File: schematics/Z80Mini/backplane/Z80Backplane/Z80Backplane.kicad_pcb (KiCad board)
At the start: 2 copper layers, 151.1 x 110.5 mm, 11 parts, among them J1 Conn_02x20_Odd_Even, J2 Conn_02x20_Odd_Even, J3 Conn_02x20_Odd_Even, J4 Conn_02x20_Odd_Even, U1 L7805

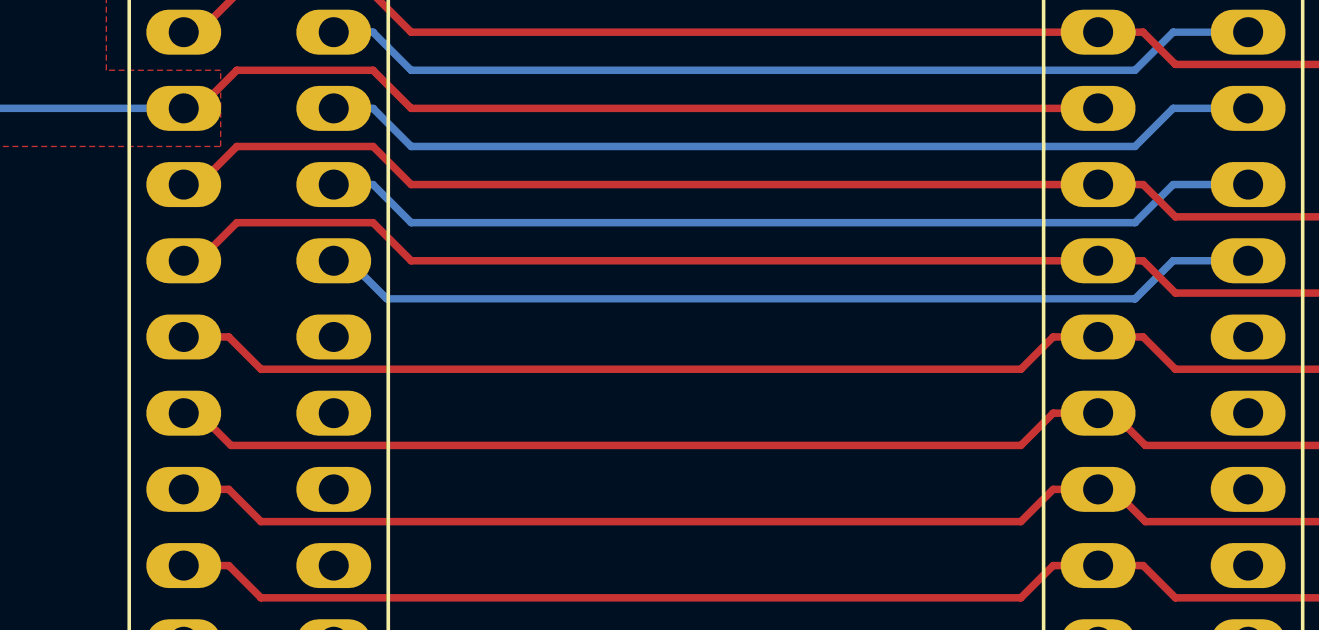
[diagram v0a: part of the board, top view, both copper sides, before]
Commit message: Added new code for core written in C with Z88DK
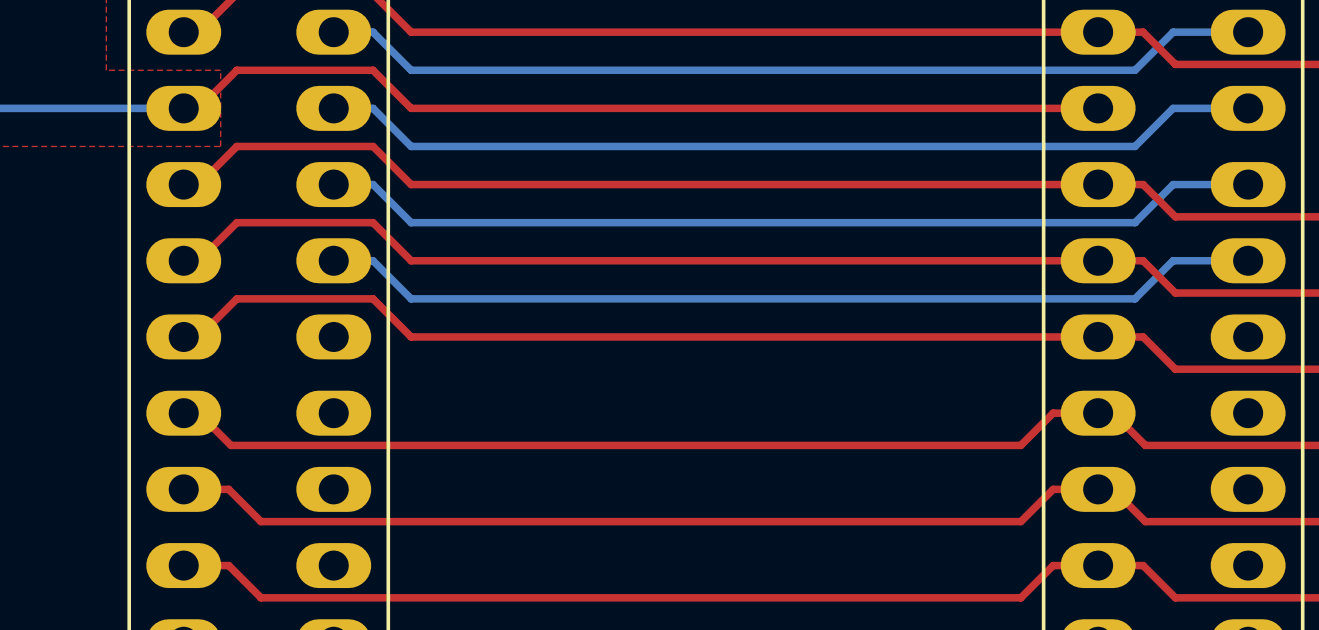
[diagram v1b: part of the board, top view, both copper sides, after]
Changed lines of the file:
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@@
-(kicad_pcb (version 20171130) (host pcbnew "(5.1.2)-1")
+(kicad_pcb (version 20171130) (host pcbnew "(5.1.4)-1")
   (general
     (thickness 1.6)
     (drawings 4)
-    (tracks 377)
+    (tracks 378)
     (zones 0)
     (modules 11)
@@
     (trace_clearance 0.2)
     (zone_clearance 0.508)
-    (zone_45_only no)
+    (zone_45_only yes)
     (trace_min 0.2)
     (via_size 0.8)
@@
   (segment (start 129.81 82.55) (end 130.88501 83.62501) (width 0.25) (layer F.Cu) (net 22))
   (segment (start 128.31 82.55) (end 129.81 82.55) (width 0.25) (layer F.Cu) (net 22))
-  (segment (start 93.79 80.01) (end 95.29 80.01) (width 0.25) (layer F.Cu) (net 24))
-  (segment (start 92.71499 81.08501) (end 93.79 80.01) (width 0.25) (layer F.Cu) (net 24))
-  (segment (start 67.38501 81.08501) (end 92.71499 81.08501) (width 0.25) (layer F.Cu) (net 24))
-  (segment (start 66.31 80.01) (end 67.38501 81.08501) (width 0.25) (layer F.Cu) (net 24))
-  (segment (start 64.81 80.01) (end 66.31 80.01) (width 0.25) (layer F.Cu) (net 24))
   (segment (start 126.81 80.01) (end 128.31 80.01) (width 0.25) (layer F.Cu) (net 24))
   (segment (start 125.73499 81.08501) (end 126.81 80.01) (width 0.25) (layer F.Cu) (net 24))
@@
   (segment (start 129.81 80.01) (end 130.88501 81.08501) (width 0.25) (layer F.Cu) (net 24))
   (segment (start 128.31 80.01) (end 129.81 80.01) (width 0.25) (layer F.Cu) (net 24))
+  (segment (start 65.31 80.01) (end 66.58 78.74) (width 0.25) (layer F.Cu) (net 24))
+  (segment (start 64.81 80.01) (end 65.31 80.01) (width 0.25) (layer F.Cu) (net 24))
+  (segment (start 66.58 78.74) (end 71.12 78.74) (width 0.25) (layer F.Cu) (net 24))
+  (segment (start 72.39 80.01) (end 95.29 80.01) (width 0.25) (layer F.Cu) (net 24))
+  (segment (start 71.12 78.74) (end 72.39 80.01) (width 0.25) (layer F.Cu) (net 24))
   (segment (start 126.81 77.47) (end 128.31 77.47) (width 0.25) (layer F.Cu) (net 26))
   (segment (start 125.73499 78.54501) (end 126.81 77.47) (width 0.25) (layer F.Cu) (net 26))
@@
   (segment (start 72.39 77.47) (end 95.29 77.47) (width 0.25) (layer F.Cu) (net 26))
   (segment (start 71.12 76.2) (end 72.39 77.47) (width 0.25) (layer F.Cu) (net 26))
-  (segment (start 70.31 77.47) (end 71.58 78.74) (width 0.25) (layer B.Cu) (net 27))
   (segment (start 69.81 77.47) (end 70.31 77.47) (width 0.25) (layer B.Cu) (net 27))
-  (segment (start 71.58 78.74) (end 96.52 78.74) (width 0.25) (layer B.Cu) (net 27))
   (segment (start 97.79 77.47) (end 100.29 77.47) (width 0.25) (layer B.Cu) (net 27))
   (segment (start 96.52 78.74) (end 97.79 77.47) (width 0.25) (layer B.Cu) (net 27))
+  (segment (start 70.31 77.47) (end 71.12 77.47) (width 0.25) (layer B.Cu) (net 27))
+  (segment (start 71.12 77.47) (end 72.39 78.74) (width 0.25) (layer B.Cu) (net 27))
+  (segment (start 72.39 78.74) (end 96.52 78.74) (width 0.25) (layer B.Cu) (net 27))
   (segment (start 126.81 74.93) (end 128.31 74.93) (width 0.25) (layer F.Cu) (net 28))
   (segment (start 125.73499 76.00501) (end 126.81 74.93) (width 0.25) (layer F.Cu) (net 28))
@@
   (segment (start 49.53 74.93) (end 48.26 76.2) (width 1) (layer F.Cu) (net 41))
   (segment (start 40.64 49.53) (end 40.64 44.45) (width 0.25) (layer F.Cu) (net 42))
-  (zone (net 7) (net_name GND) (layer B.Cu) (hatch edge 0.508)
+  (zone (net 7) (net_name GND) (layer B.Cu) (hatch none 0.508)
     (connect_pads (clearance 0.508))
     (min_thickness 0.254)

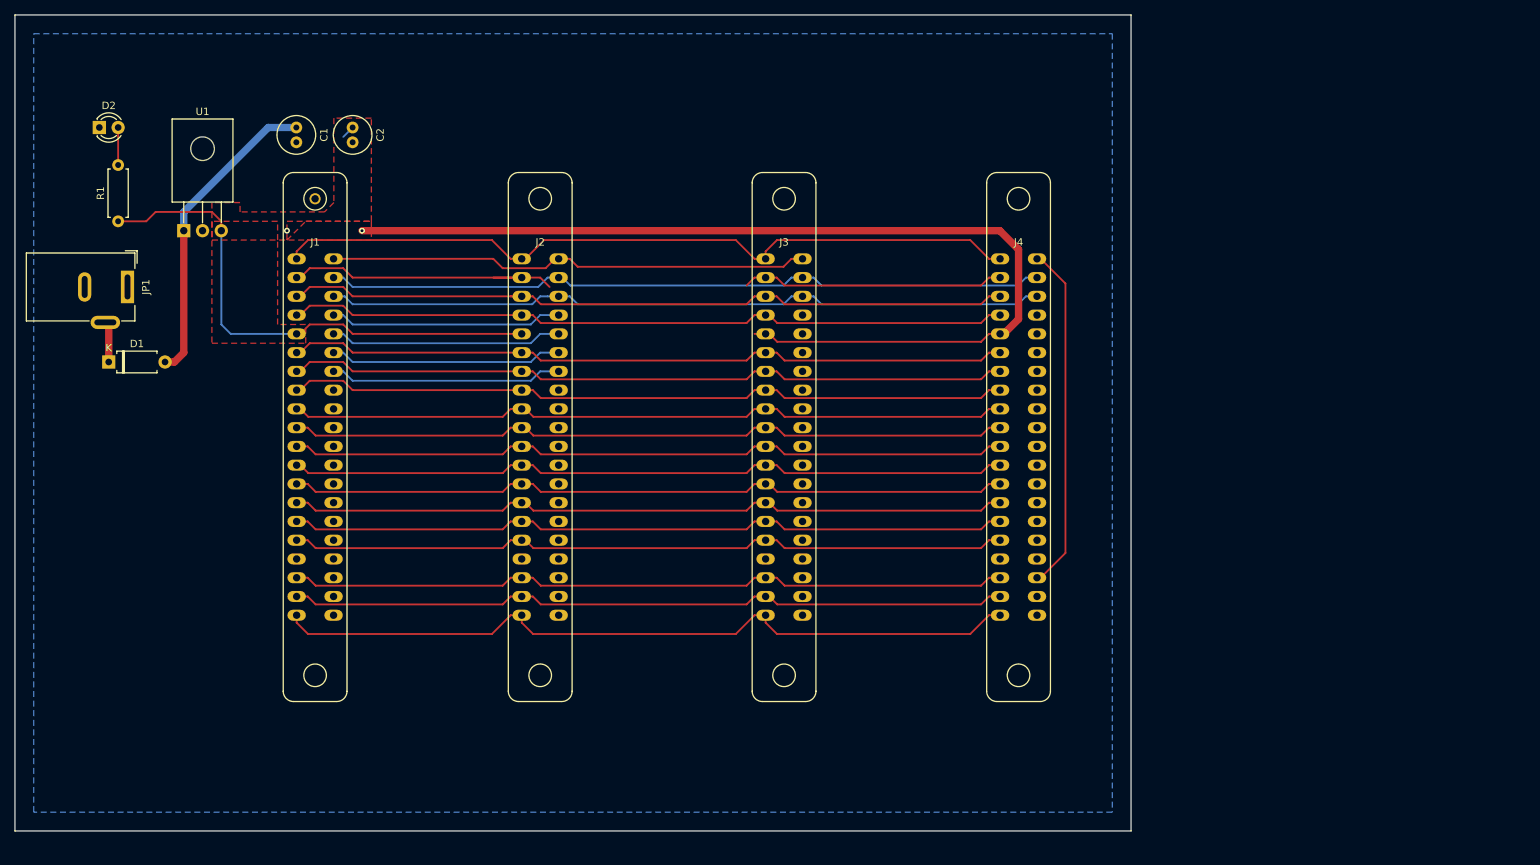
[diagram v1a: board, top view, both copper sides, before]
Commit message: Testing C routines for VDP and keyboard. Generated backplane gerber files
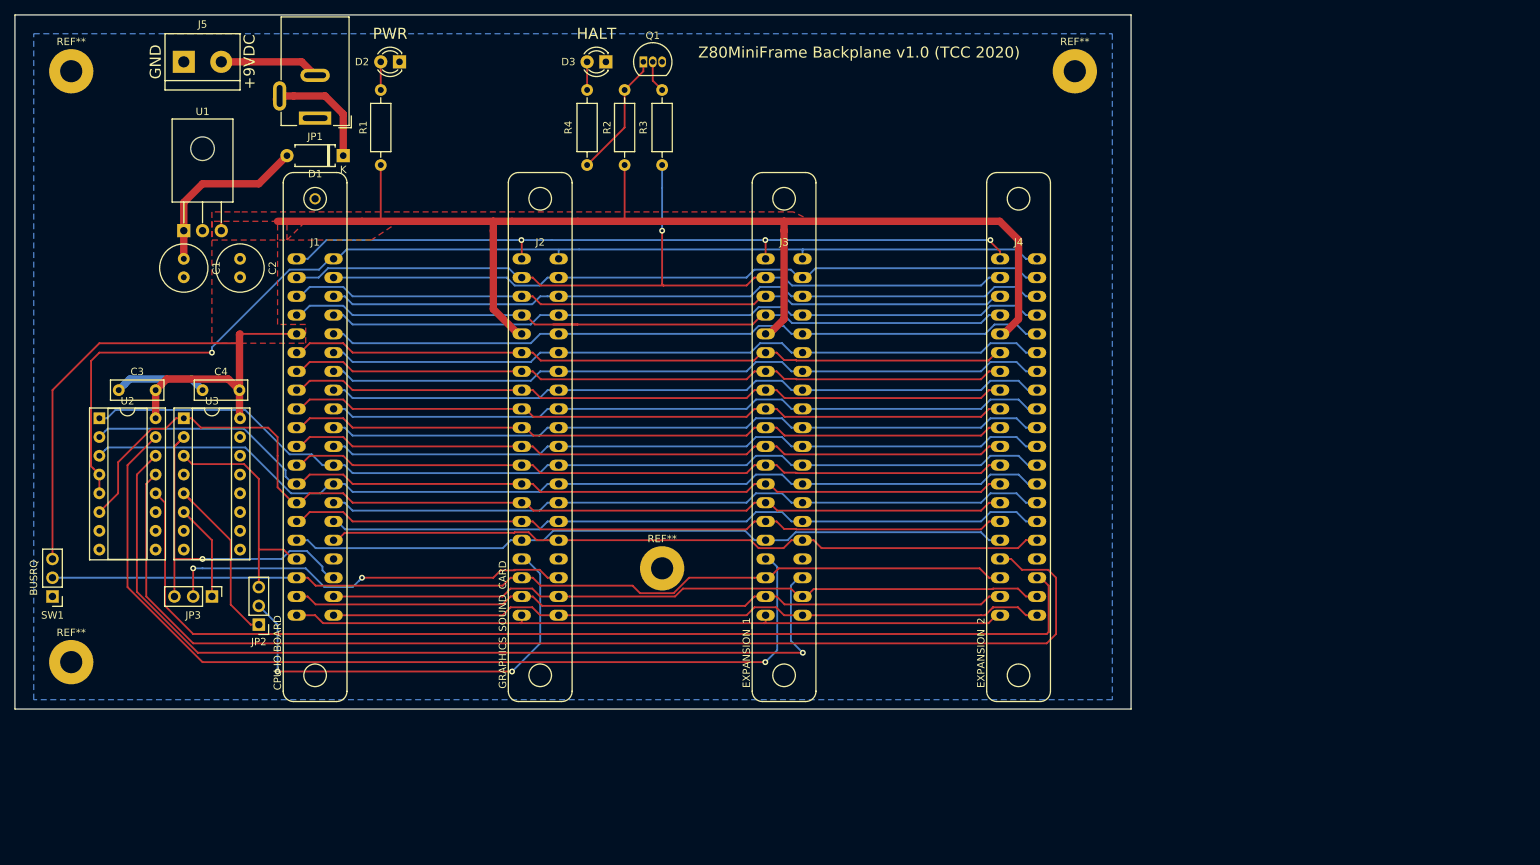
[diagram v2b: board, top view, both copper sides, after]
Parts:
- added C3: 100nF, Capacitor_THT:C_Disc_D7.0mm_W2.5mm_P5.00mm, F.Cu at (40.7, 80.0)
- added C4: 100nF, Capacitor_THT:C_Disc_D7.0mm_W2.5mm_P5.00mm, F.Cu at (52.1, 80.0)
- added D3: LED_HALT, LED_THT:LED_D3.0mm, F.Cu at (106.7, 35.6)
- added J5: Screw_Terminal_01x02, TerminalBlock:TerminalBlock_bornier-2_P5.08mm, F.Cu at (49.5, 35.6)
- added JP2: Jumper_NC_Dual, Connector_PinHeader_2.54mm:PinHeader_1x03_P2.54mm_Vertical, F.Cu at (59.7, 111.8)
- added JP3: Jumper_NC_Dual, Connector_PinHeader_2.54mm:PinHeader_1x03_P2.54mm_Vertical, F.Cu at (53.3, 108.0)
- added Q1: BC337, Package_TO_SOT_THT:TO-92_Inline, F.Cu at (111.8, 35.6)
- added R2: 330R, Resistor_THT:R_Axial_DIN0207_L6.3mm_D2.5mm_P10.16mm_Horizontal, F.Cu at (109.2, 49.5)
- added R3: 1K, Resistor_THT:R_Axial_DIN0207_L6.3mm_D2.5mm_P10.16mm_Horizontal, F.Cu at (114.3, 39.4)
- added R4: 330R, Resistor_THT:R_Axial_DIN0207_L6.3mm_D2.5mm_P10.16mm_Horizontal, F.Cu at (104.1, 39.4)
- added REF**: MountingHole_3mm_Pad, MountingHole:MountingHole_3mm_Pad, F.Cu at (114.3, 104.1)
- added REF**: MountingHole_3mm_Pad, MountingHole:MountingHole_3mm_Pad, F.Cu at (34.3, 116.8)
- added REF**: MountingHole_3mm_Pad, MountingHole:MountingHole_3mm_Pad, F.Cu at (34.3, 36.8)
- added REF**: MountingHole_3mm_Pad, MountingHole:MountingHole_3mm_Pad, F.Cu at (170.2, 36.8)
- added SW1: SW_SPDT, Connector_PinHeader_2.54mm:PinHeader_1x03_P2.54mm_Vertical, F.Cu at (31.8, 108.0)
- added U2: 74LS138, Package_DIP:DIP-16_W7.62mm_Socket, F.Cu at (38.1, 83.8)
- added U3: 74LS139, Package_DIP:DIP-16_W7.62mm_Socket, F.Cu at (49.5, 83.8)
- C1, C2: footprint Capacitor_THT:C_Radial_D5.0mm_H11.0mm_P2.00mm -> Capacitor_THT:C_Radial_D6.3mm_H5.0mm_P2.50mm
- J1: value Conn_02x20_Odd_Even -> CPU-IO BOARD
- J2: value Conn_02x20_Odd_Even -> GRAPHICS_SOUND_CARD
- J3: value Conn_02x20_Odd_Even -> EXPANSION_1
- J4: value Conn_02x20_Odd_Even -> EXPANSION_2
- R1: footprint Resistor_THT:R_Axial_DIN0207_L6.3mm_D2.5mm_P7.62mm_Horizontal -> Resistor_THT:R_Axial_DIN0207_L6.3mm_D2.5mm_P10.16mm_Horizontal
- moved D1 42.3 mm to (71.1, 48.3), turned to 180 degrees
- moved D2 41.6 mm to (78.7, 35.6), turned to 180 degrees
- moved R1 36.4 mm to (76.2, 49.5)
- moved JP1 34.2 mm to (67.3, 43.2), turned to 180 degrees
- moved C2 23.4 mm to (57.1, 62.2)
- moved C1 23.4 mm to (49.5, 62.2)
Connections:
- J1 pad 33: GND -> /VDP_SEL
- J1 pad 36: /IORQ -> /SND_SEL
- J2 pad 33: GND -> Net-(J2-Pad33)
- J2 pad 36: /IORQ -> Net-(J2-Pad36)
- J3 pad 33: GND -> Net-(J3-Pad33)
- J3 pad 36: /IORQ -> Net-(J3-Pad36)
- J4 pad 33: GND -> Net-(J4-Pad33)
- J4 pad 36: /IORQ -> Net-(J4-Pad36)
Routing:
- net Net-(J4-Pad33): track 0.00 -> 160.1 mm
- net Net-(J4-Pad36): track 0.00 -> 145.9 mm
- net /A7: track 0.00 -> 135.0 mm
- net /A5: track 0.00 -> 134.5 mm
- net Net-(J3-Pad33): track 0.00 -> 128.1 mm, vias 0 -> 1
- net Net-(J3-Pad36): track 0.00 -> 124.8 mm, vias 0 -> 1
- net /A11: track 0.00 -> 100.2 mm
- net /BUSACK: track 0.00 -> 99.9 mm
- net /WR: track 0.00 -> 99.7 mm
- net /A3: track 0.00 -> 99.7 mm
- net /D6: track 0.00 -> 99.7 mm
- net /A14: track 0.00 -> 99.4 mm
- net /A9: track 0.00 -> 99.2 mm
- net /A1: track 0.00 -> 99.2 mm
- net /INT: track 0.00 -> 99.0 mm
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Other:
- board size 151.1 x 110.5 mm -> 151.1 x 94 mm
- board text added: "+9VDC"
- board text added: "BUSRQ"
- board text added: "GND"
- board text added: "HALT"
- board text added: "PWR"
- board text added: "Z80MiniFrame Backplane v1.0 (TCC 2020)"

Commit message: Latest changes and added CTC initialization and routine to flash cursor
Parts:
- moved J4 3.81 mm to (158.8, 86.4)
- moved J3 2.54 mm to (128.3, 86.4)
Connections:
- J1 pad 2: /IORQ -> /NMI
- J1 pad 4: /NMI -> /WAIT
- J1 pad 6: /WAIT -> /IORQ
- J2 pad 2: /IORQ -> /NMI
- J2 pad 4: /NMI -> /WAIT
- J2 pad 6: /WAIT -> /IORQ
- J3 pad 2: /IORQ -> /NMI
- J3 pad 4: /NMI -> /WAIT
- J3 pad 6: /WAIT -> /IORQ
- J4 pad 2: /IORQ -> /NMI
- J4 pad 4: /NMI -> /WAIT
- J4 pad 6: /WAIT -> /IORQ
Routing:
- net Net-(J4-Pad33): track 160.1 -> 26.0 mm
- net Net-(J4-Pad36): track 145.9 -> 21.2 mm
- net /WR: track 99.7 -> 57.3 mm
- net /A1: track 99.2 -> 57.3 mm
- net /IORQ: track 157.2 -> 117.6 mm
- net /A7: track 135.0 -> 96.2 mm
- net /A9: track 99.2 -> 60.9 mm
- net /A3: track 99.7 -> 62.4 mm
- net /D6: track 99.7 -> 63.2 mm
- net /M1: track 103.6 -> 67.4 mm
- net /D4: track 99.4 -> 63.4 mm
- net /RD: track 99.7 -> 63.9 mm
- net /D2: track 98.4 -> 63.1 mm
- net /RESET: track 98.7 -> 63.4 mm
- net /A5: track 134.5 -> 99.3 mm
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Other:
- board text added: "Z80MiniFrame Backplane v1.1 (TCC 2020)"
- board text removed: "Z80MiniFrame Backplane v1.0 (TCC 2020)"
